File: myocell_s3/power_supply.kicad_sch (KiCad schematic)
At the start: 19 parts, among them Q3 DMG3404L, SW3 SW_Nidec_CAS-120A1, U6 AP2112K-3.3, U7 MCP73831-2-OT, U8 AP2112K-3.3

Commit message: RLDINV still unconnected
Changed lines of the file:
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@@
 			)
 		)
-		(property "Description" ""
+		(property "Description" "Resistor, US symbol"
 			(at 127 85.09 0)
 			(effects
@@
 			)
 		)
-		(property "Description" ""
+		(property "Description" "600mA low dropout linear regulator, with enable pin, 3.8V-6V input voltage range, 3.3V fixed positive output, SOT-23-5"
 			(at 134.62 147.32 0)
 			(effects
@@
 			)
 		)
-		(property "Description" ""
+		(property "Description" "Power symbol creates a global label with name \"GND\" , ground"
 			(at 73.66 91.44 0)
 			(effects
@@
 			)
 		)
-		(property "Description" ""
+		(property "Description" "Unpolarized capacitor"
 			(at 105.41 82.55 0)
 			(effects
@@
 			)
 		)
-		(property "Description" ""
+		(property "Description" "Power symbol creates a global label with name \"GND\" , ground"
 			(at 162.56 71.12 0)
 			(effects
@@
 			)
 		)
-		(property "Description" ""
+		(property "Description" "Power symbol creates a global label with name \"GND\" , ground"
 			(at 78.74 154.94 0)
 			(effects
@@
 			)
 		)
-		(property "Description" ""
+		(property "Description" "Resistor, US symbol"
 			(at 127 95.25 0)
 			(effects
@@
 			)
 		)
-		(property "Description" ""
+		(property "Description" "Power symbol creates a global label with name \"GND\" , ground"
 			(at 64.77 154.94 0)
 			(effects
@@
 			)
 		)
-		(property "Description" ""
+		(property "Description" "Power symbol creates a global label with name \"GND\" , ground"
 			(at 85.09 91.44 0)
 			(effects
@@
 			)
 		)
-		(property "Description" ""
+		(property "Description" "Switch, single pole double throw"
 			(at 171.45 50.8 0)
 			(effects
@@
 			)
 		)
-		(property "Description" ""
+		(property "Description" "Power symbol creates a global label with name \"GND\" , ground"
 			(at 91.44 154.94 0)
 			(effects
@@
 			)
 		)
-		(property "Description" ""
+		(property "Description" "Resistor, US symbol"
 			(at 121.92 67.31 0)
 			(effects
@@
 			)
 		)
-		(property "Description" ""
+		(property "Description" "5.8A Id, 30V Vds, N-Channel MOSFET, SOT-23"
 			(at 133.35 68.58 0)
 			(effects
@@
 			)
 		)
-		(property "Description" ""
+		(property "Description" "Power symbol creates a global label with name \"GND\" , ground"
 			(at 121.92 71.12 0)
 			(effects
@@
 			)
 		)
-		(property "Description" ""
+		(property "Description" "Power symbol creates a global label with name \"GND\" , ground"
 			(at 119.38 156.21 0)
 			(effects
@@
 			)
 		)
-		(property "Description" ""
+		(property "Description" "600mA low dropout linear regulator, with enable pin, 3.8V-6V input voltage range, 3.3V fixed positive output, SOT-23-5"
 			(at 78.74 146.05 0)
 			(effects
@@
 			)
 		)
-		(property "Description" ""
+		(property "Description" "Unpolarized capacitor"
 			(at 147.32 149.86 0)
 			(effects
@@
 			)
 		)
-		(property "Description" ""
+		(property "Description" "Power symbol creates a global label with name \"GND\" , ground"
 			(at 127 100.33 0)
 			(effects
@@
 			)
 		)
-		(property "Description" ""
+		(property "Description" "Power symbol creates a global label with name \"GND\" , ground"
 			(at 68.58 76.2 0)
 			(effects
@@
 			)
 		)
-		(property "Description" ""
+		(property "Description" "Unpolarized capacitor"
 			(at 162.56 67.31 0)
 			(effects
@@
 			)
 		)
-		(property "Description" ""
+		(property "Description" "Power symbol creates a global label with name \"GND\" , ground"
 			(at 134.62 156.21 0)
 			(effects
@@
 			)
 		)
-		(property "Description" ""
+		(property "Description" "Power symbol creates a global label with name \"GND\" , ground"
 			(at 158.75 48.26 0)
 			(effects
@@
 			)
 		)
-		(property "Description" ""
+		(property "Description" "Light emitting diode"
+			(at 97.79 88.9 0)
+			(effects
+				(font
+					(size 1.27 1.27)
+				)
+				(hide yes)
+			)
+		)
+		(property "Sim.Pins" "1=K 2=A"
 			(at 97.79 88.9 0)
 			(effects
@@
 			)
 		)
-		(property "Description" ""
+		(property "Description" "Unpolarized capacitor"
 			(at 68.58 69.85 0)
 			(effects
@@
 			)
 		)
-		(property "Description" ""
+		(property "Description" "Resistor, US symbol"
 			(at 73.66 87.63 0)
 			(effects
@@
 			)
 		)
-		(property "Description" ""
+		(property "Description" "Unpolarized capacitor"
 			(at 64.77 149.86 0)
 			(effects
@@
 			)
 		)
-		(property "Description" ""
+		(property "Description" "Power symbol creates a global label with name \"GND\" , ground"
 			(at 105.41 91.44 0)
 			(effects
@@
 			)
 		)
-		(property "Description" ""
+		(property "Description" "Single cell, Li-Ion/Li-Po charge management controller, 4.20V, Tri-State Status Output, in SOT23-5 package"
 			(at 85.09 80.01 0)
 			(effects
@@
 			)
 		)
-		(property "Description" ""
+		(property "Description" "Resistor, US symbol"
 			(at 97.79 96.52 0)
 			(effects
@@
 			)
 		)
-		(property "Description" ""
+		(property "Description" "Unpolarized capacitor"
 			(at 91.44 149.86 0)
 			(effects
@@
 			)
 		)
-		(property "Description" ""
+		(property "Description" "Unpolarized capacitor"
 			(at 119.38 149.86 0)
 			(effects

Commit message: MSS22D18 slider switch added
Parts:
- removed SW3: SW_Nidec_CAS-120A1, Button_Switch_SMD:Nidec_Copal_CAS-120A, symbol Switch:SW_Nidec_CAS-120A1
- added U1: MSS22D18, symbol myocell_s3:MSS22D18
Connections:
- net GND: now also U1.1
- net PWR_ENA: now also U1.2
- net VIN: now also U1.3
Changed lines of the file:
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@@
 	(wire
 		(pts
-			(xy 105.41 86.36) (xy 105.41 91.44)
+			(xy 158.75 48.26) (xy 161.29 48.26)
 		)
 		(stroke
@@
 	(wire
 		(pts
-			(xy 125.73 148.59) (xy 125.73 147.32)
+			(xy 105.41 86.36) (xy 105.41 91.44)
 		)
 		(stroke
@@
 	(wire
 		(pts
-			(xy 147.32 153.67) (xy 147.32 156.21)
+			(xy 125.73 148.59) (xy 125.73 147.32)
 		)
 		(stroke
@@
 	(wire
 		(pts
-			(xy 166.37 53.34) (xy 162.56 53.34)
+			(xy 147.32 153.67) (xy 147.32 156.21)
 		)
 		(stroke
@@
 	(wire
 		(pts
+			(xy 158.75 50.8) (xy 171.45 50.8)
+		)
+		(stroke
+			(width 0)
+			(type default)
+		)
+	)
+	(wire
+		(pts
 			(xy 64.77 143.51) (xy 71.12 143.51)
 		)
@@
 	(wire
 		(pts
-			(xy 176.53 50.8) (xy 180.34 50.8)
+			(xy 158.75 53.34) (xy 162.56 53.34)
 		)
 		(stroke
@@
 	(wire
 		(pts
-			(xy 158.75 48.26) (xy 166.37 48.26)
-		)
-		(stroke
-			(width 0)
-			(type default)
-		)
-	)
-	(wire
-		(pts
 			(xy 91.44 143.51) (xy 87.63 143.51)
 		)
@@
 	(global_label "PWR_ENA"
 		(shape input)
-		(at 180.34 50.8 0)
+		(at 171.45 50.8 0)
 		(fields_autoplaced yes)
 		(effects
@@
 		)
 		(property "Intersheetrefs" "${INTERSHEET_REFS}"
-			(at 191.8523 50.8 0)
+			(at 182.9623 50.8 0)
 			(effects
 				(font
@@
 	)
 	(symbol
-		(lib_id "Switch:SW_Nidec_CAS-120A1")
-		(at 171.45 50.8 180)
-		(unit 1)
-		(exclude_from_sim no)
-		(in_bom yes)
-		(on_board yes)
-		(dnp no)
-		(fields_autoplaced yes)
-		(property "Reference" "SW3"
-			(at 171.3865 43.18 0)
-			(effects
-				(font
-					(size 1.27 1.27)
-				)
-			)
-		)
-		(property "Value" "SW_Nidec_CAS-120A1"
-			(at 171.3865 45.72 0)
-			(effects
-				(font
-					(size 1.27 1.27)
-				)
-			)
-		)
-		(property "Footprint" "Button_Switch_SMD:Nidec_Copal_CAS-120A"
-			(at 171.45 40.64 0)
-			(effects
-				(font
-					(size 1.27 1.27)
-				)
-				(hide yes)
-			)
-		)
-		(property "Datasheet" "https://www.nidec-components.com/e/catalog/switch/cas.pdf"
-			(at 171.45 43.18 0)
-			(effects
-				(font
-					(size 1.27 1.27)
-				)
-				(hide yes)
-			)
-		)
-		(property "Description" "Switch, single pole double throw"
-			(at 171.45 50.8 0)
-			(effects
-				(font
-					(size 1.27 1.27)
-				)
-				(hide yes)
-			)
-		)
-		(pin "2"
-		)
-		(pin "1"
-		)
-		(pin "3"
-		)
-		(instances
-			(project "myocell2"
-				(path "/871ff10b-bde5-471c-b91a-de58aa271388/e36bfe9c-db3d-4e13-afda-f7f295377ecb"
-					(reference "SW3")
-					(unit 1)
-				)
-			)
-			(project "myocell2"
-				(path "/e513cd5e-988e-4071-93cd-c2c2c010dd7c/eca13eb4-a680-4456-b37c-b91993f488a3"
-					(reference "SW?")
-					(unit 1)
-				)
-			)
-			(project "ADS1292EMG2x"
-				(path "/e63e39d7-6ac0-4ffd-8aa3-1841a4541b55/46ace08d-eb32-49ac-809d-2e61e71dabf9"
-					(reference "SW?")
-					(unit 1)
-				)
-			)
-		)
-	)
-	(symbol
 		(lib_id "power:GND")
 		(at 91.44 154.94 0)
@@
 	(symbol
 		(lib_id "power:GND")
-		(at 158.75 48.26 270)
+		(at 161.29 48.26 90)
 		(unit 1)
 		(exclude_from_sim no)
@@
 		(dnp no)
 		(property "Reference" "#PWR076"
-			(at 152.4 48.26 0)
+			(at 167.64 48.26 0)
 			(effects
 				(font
@@
 		)
 		(property "Value" "GND"
-			(at 154.94 45.72 0)
+			(at 169.164 48.26 90)
 			(effects
 				(font
@@
 		)
 		(property "Footprint" ""
-			(at 158.75 48.26 0)
+			(at 161.29 48.26 0)
 			(effects
 				(font
@@
 		)
 		(property "Datasheet" ""
-			(at 158.75 48.26 0)
+			(at 161.29 48.26 0)
 			(effects
 				(font
@@
 		)
 		(property "Description" "Power symbol creates a global label with name \"GND\" , ground"
-			(at 158.75 48.26 0)
+			(at 161.29 48.26 0)
 			(effects
 				(font
@@
 					(unit 1)
 				)
+			)
+		)
+	)
+	(symbol
+		(lib_id "myocell_s3:MSS22D18")
+		(at 154.94 50.8 270)
+		(unit 1)
+		(exclude_from_sim no)
+		(in_bom yes)
+		(on_board yes)
+		(dnp no)
+		(property "Reference" "U1"
+			(at 154.178 45.466 90)
+			(effects
+				(font
+					(size 1.27 1.27)
+				)
+			)
+		)
+		(property "Value" "MSS22D18"
+			(at 153.67 56.642 90)
+			(effects
+				(font
+					(size 1.27 1.27)
+				)
+			)
+		)
+		(property "Footprint" ""
+			(at 154.94 50.8 0)
+			(effects
+				(font
+					(size 1.27 1.27)
+				)
+				(hide yes)
+			)
+		)
+		(property "Datasheet" ""
+			(at 154.94 50.8 0)
+			(effects
+				(font
+					(size 1.27 1.27)
+				)
+				(hide yes)
+			)
+		)
+		(property "Description" ""
+			(at 154.94 50.8 0)
+			(effects
+				(font
+					(size 1.27 1.27)
+				)
+				(hide yes)
+			)
+		)
+		(pin "5"
+		)
+		(pin "2"
+		)
+		(pin "4"
+		)
+		(pin "1"
+		)
+		(pin "6"
+		)
+		(pin "3"
+		)
+		(instances
+			(project ""
+				(path "/871ff10b-bde5-471c-b91a-de58aa271388/e36bfe9c-db3d-4e13-afda-f7f295377ecb"
+					(reference "U1")
+					(unit 1)
+				)

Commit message: schematic and footprints done
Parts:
- U1: footprint (none) -> emg:MSS22D18
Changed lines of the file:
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@@
 			)
 		)
-		(property "Footprint" ""
+		(property "Footprint" "emg:MSS22D18"
 			(at 154.94 50.8 0)
 			(effects

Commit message: working on parts placement
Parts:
- R25: value 1k -> 2k
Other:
- note added: "Fast charge current regulation can be scaled by placing a programming resistor (RPROG) from the PROG input to VSS. The program resistor and the charge current are calculated using the following equation (MCP73831/2: https://static.chipdip.ru/lib/283/DOC012283193.pdf) I_{REG}=1000V/R_{PROG}"
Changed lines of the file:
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@@
 		(company "MIREA/Rf-lab.org")
+	)
+	(text "Fast charge current regulation can be scaled by placing\na programming resistor (RPROG) from the PROG input\nto VSS. The program resistor and the charge current\nare calculated using the following equation \n(MCP73831/2: https://static.chipdip.ru/lib/283/DOC012283193.pdf)\nI_{REG}=1000V/R_{PROG}"
+		(exclude_from_sim no)
+		(at 72.136 111.76 0)
+		(effects
+			(font
+				(size 1.27 1.27)
+			)
+		)
 	)
 	(text "Analog 3.3v"
@@
 			)
 		)
-		(property "Value" "1k"
+		(property "Value" "2k"
 			(at 69.85 88.9 0)
 			(effects

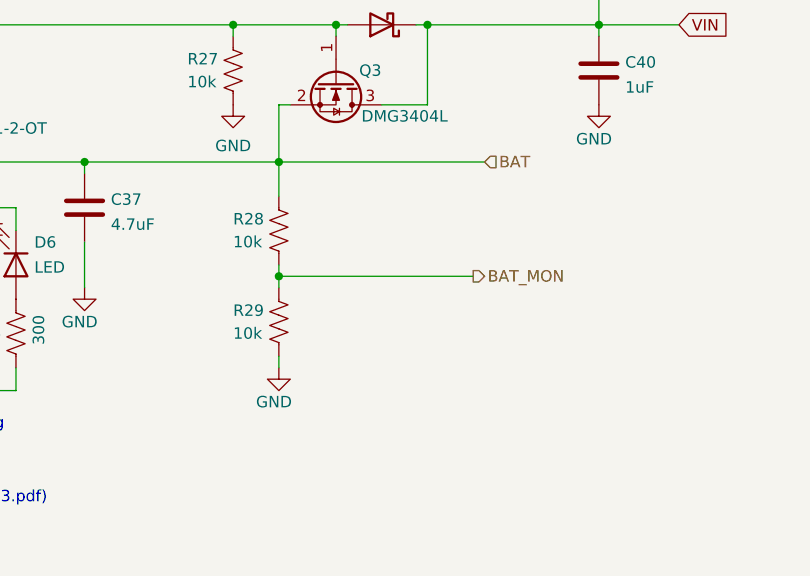
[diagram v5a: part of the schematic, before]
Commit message: placing polygons
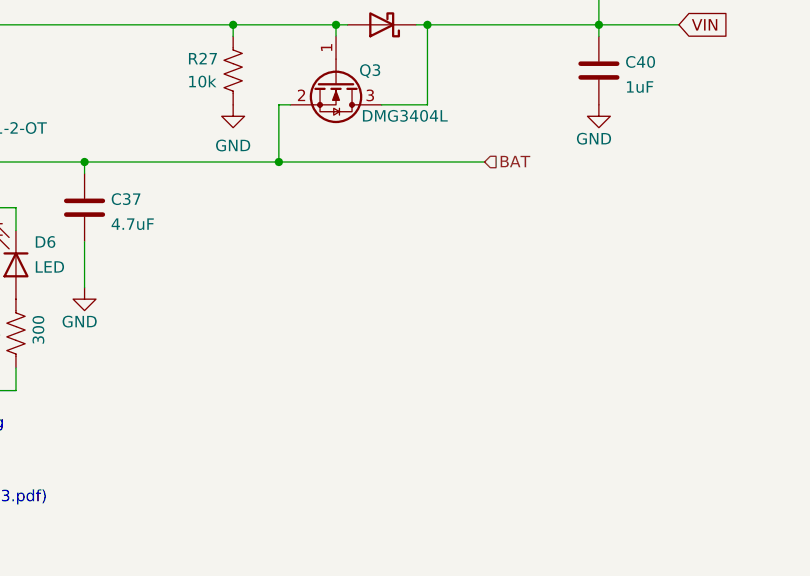
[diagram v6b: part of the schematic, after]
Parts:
- removed R28, R29: 10k, Resistor_SMD:R_0805_2012Metric_Pad1.20x1.40mm_HandSolder, symbol Device:R_US

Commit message: DRC
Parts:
- added R28, R29: 10k, Resistor_SMD:R_0805_2012Metric_Pad1.20x1.40mm_HandSolder, symbol Device:R_US
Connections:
- net BAT: now also R28.2
- net GND: now also R29.1
- new net bat_mon: R28.1, R29.2
